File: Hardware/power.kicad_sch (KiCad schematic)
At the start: 27 parts, among them J3 XT30, Q1 FDN340P, Q2 FDN340P, U10 LTC4412, U6 MP2331, U7 KA78M05, U9 LTC4412

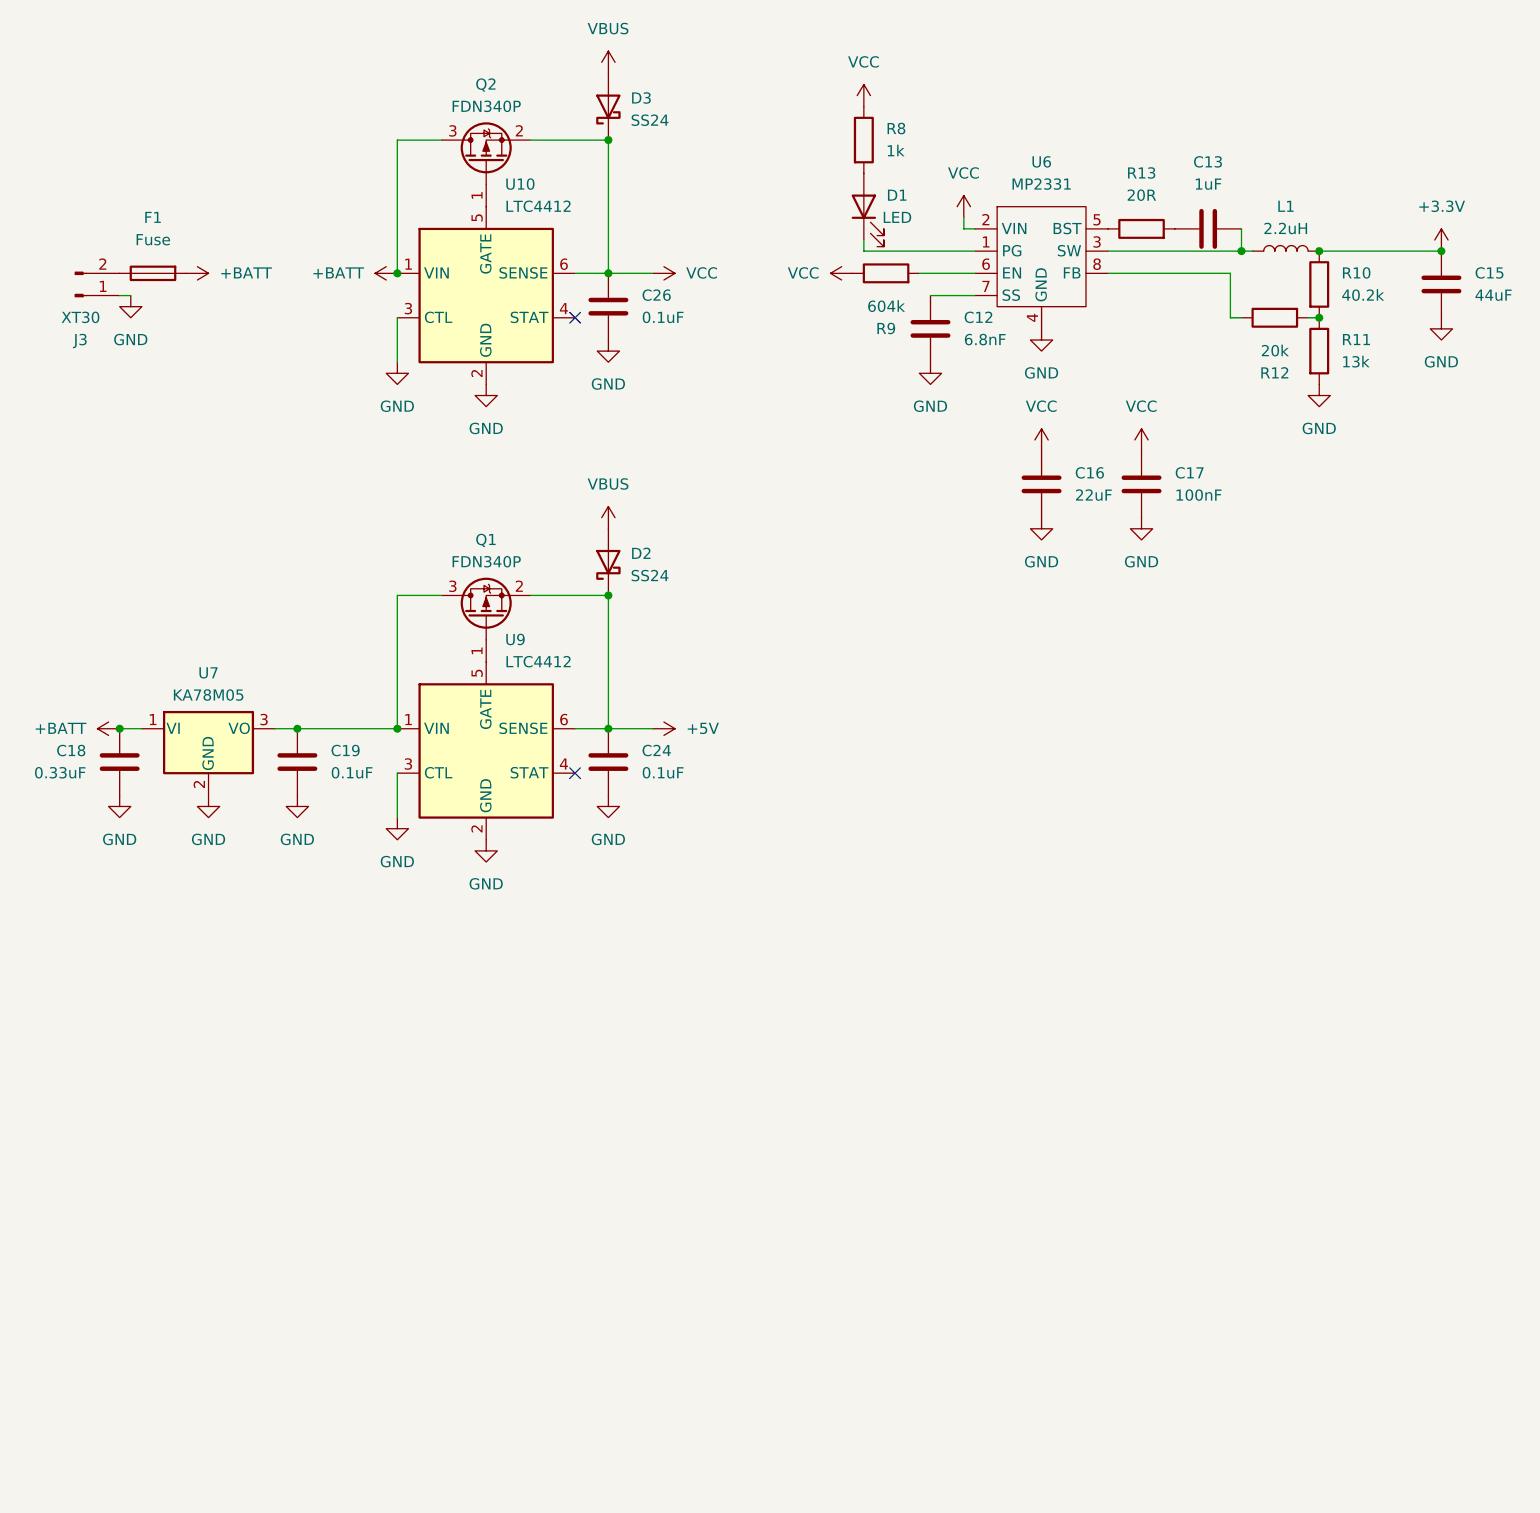
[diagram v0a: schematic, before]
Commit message: Ignition system added
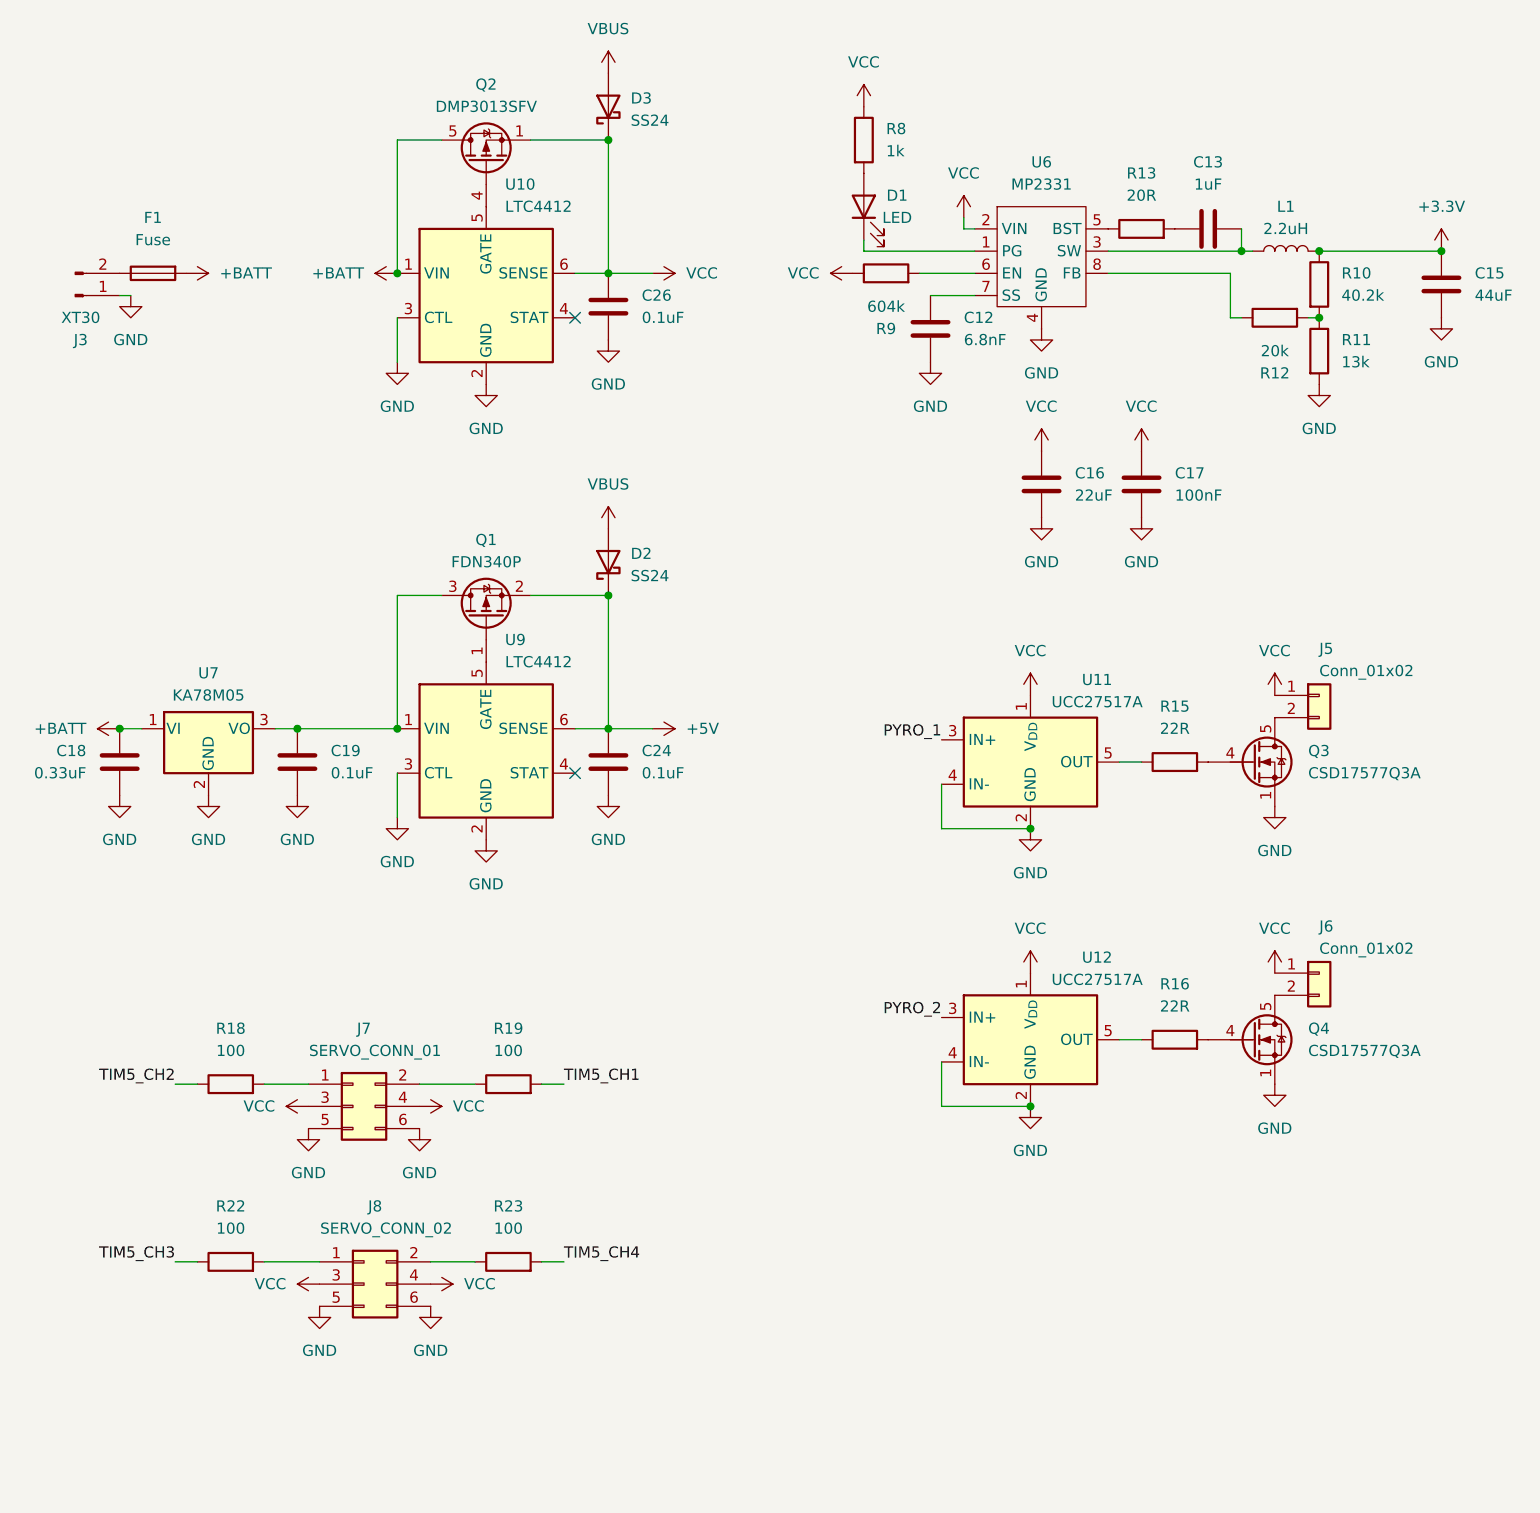
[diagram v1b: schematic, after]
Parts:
- removed Q2: FDN340P, Package_TO_SOT_SMD:SOT-23, symbol Transistor_FET:FDN340P
- added J5, J6: Conn_01x02, TerminalBlock_4Ucon:TerminalBlock_4Ucon_1x02_P3.50mm_Vertical, symbol Connector_Generic:Conn_01x02
- added J7: SERVO_CONN_01, Connector_PinHeader_2.54mm:PinHeader_2x03_P2.54mm_Vertical, symbol Connector_Generic:Conn_02x03_Odd_Even
- added J8: SERVO_CONN_02, Connector_PinHeader_2.54mm:PinHeader_2x03_P2.54mm_Vertical, symbol Connector_Generic:Conn_02x03_Odd_Even
- added Q2: DMP3013SFV, Package_SON:Diodes_PowerDI3333-8, symbol Transistor_FET:DMP3013SFV
- added Q3, Q4: CSD17577Q3A, Package_SON:VSON-8_3.3x3.3mm_P0.65mm_NexFET, symbol Transistor_FET:CSD17577Q3A
- added R15, R16: 22R, symbol Device:R
- added R18, R19, R22, R23: 100, Resistor_SMD:R_0402_1005Metric, symbol Device:R
- added U11, U12: UCC27517A, Package_TO_SOT_SMD:SOT-23-5, symbol library:UCC27517A
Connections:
- net +BATT: now also Q2.5 (D)
- net GND: now also J7.5 (Pin_5), J7.6 (Pin_6), J8.5 (Pin_5), J8.6 (Pin_6), Q3.1 (S), Q3.2 (S), Q3.3 (S), Q4.1 (S), Q4.2 (S), Q4.3 (S), U11.2 (GND), U11.4 (IN-), U12.2 (GND), U12.4 (IN-)
- net VCC: now also J5.1 (Pin_1), J6.1 (Pin_1), J7.3 (Pin_3), J7.4 (Pin_4), J8.3 (Pin_3), J8.4 (Pin_4), Q2.1 (S), Q2.2 (S), Q2.3 (S), U11.1 (V_{DD}), U12.1 (V_{DD})
- net at U10.5 (GATE): now also Q2.4 (G)
- new net: J5.2 (Pin_2), Q3.5 (D)
- new net: J7.2 (Pin_2), R19.1
- new net: J6.2 (Pin_2), Q4.5 (D)
- new net: J8.1 (Pin_1), R22.2
- new net: Q4.4 (G), R16.2
- new net: J7.1 (Pin_1), R18.2
- new net: Q3.4 (G), R15.2
- new net: R16.1, U12.5 (OUT)
- new net: R15.1, U11.5 (OUT)
- new net: J8.2 (Pin_2), R23.1
- new net PYRO_1: U11.3 (IN+)
- new net PYRO_2: U12.3 (IN+)
- new net TIM5_CH1: R19.2
- new net TIM5_CH2: R18.1
- new net TIM5_CH3: R22.1
- new net TIM5_CH4: R23.2

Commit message: vnk commitoju vēlreiz
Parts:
- added J9: SERVO_CONN_02, Connector_PinHeader_2.54mm:PinHeader_2x03_P2.54mm_Vertical, symbol Connector_Generic:Conn_02x03_Odd_Even
- added R17, R20: 100, Resistor_SMD:R_0402_1005Metric, symbol Device:R
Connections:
- net GND: now also J9.5 (Pin_5), J9.6 (Pin_6)
- net VCC: now also J9.3 (Pin_3), J9.4 (Pin_4)
- new net: J9.1 (Pin_1), R17.2
- new net: J9.2 (Pin_2), R20.1
- new net TIM4_CH3: R17.1
- new net TIM4_CH4: R20.2
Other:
- moved on the sheet: J7, J8, R18, R19, R22, R23
